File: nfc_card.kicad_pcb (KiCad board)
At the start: 2 copper layers, 2 parts, among them IC1 NT3H2111W0FHKH

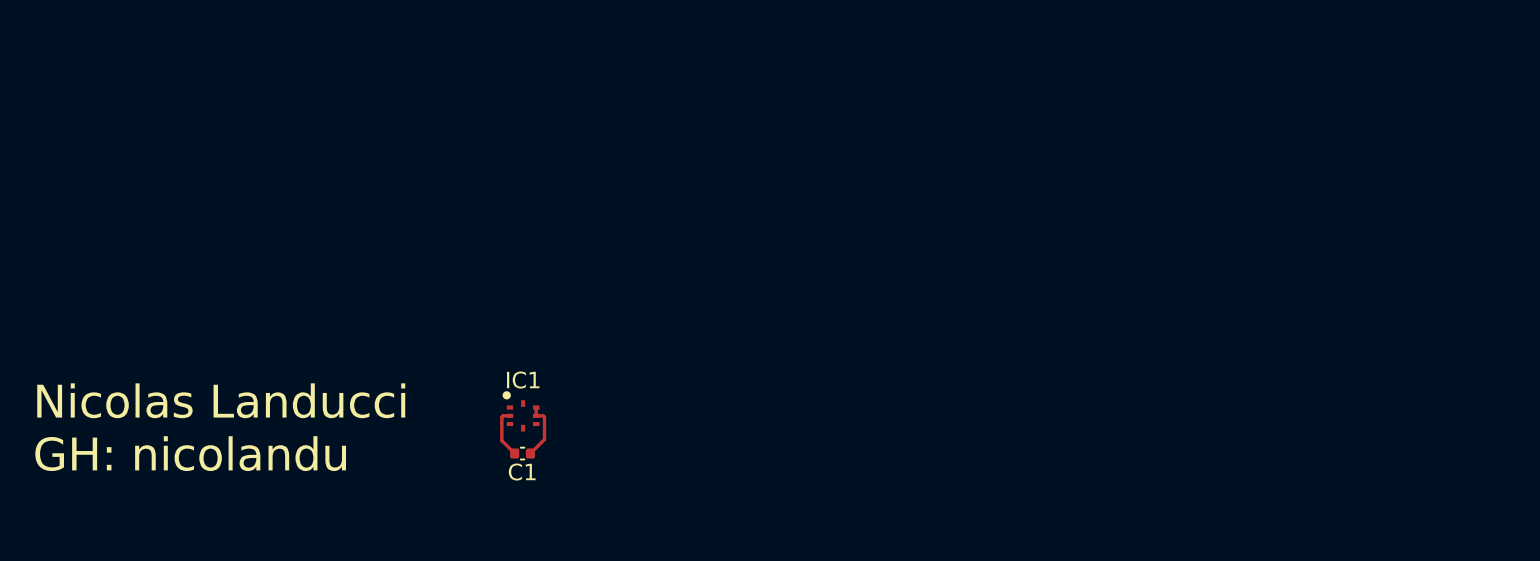
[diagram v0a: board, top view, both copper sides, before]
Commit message: Add antenna
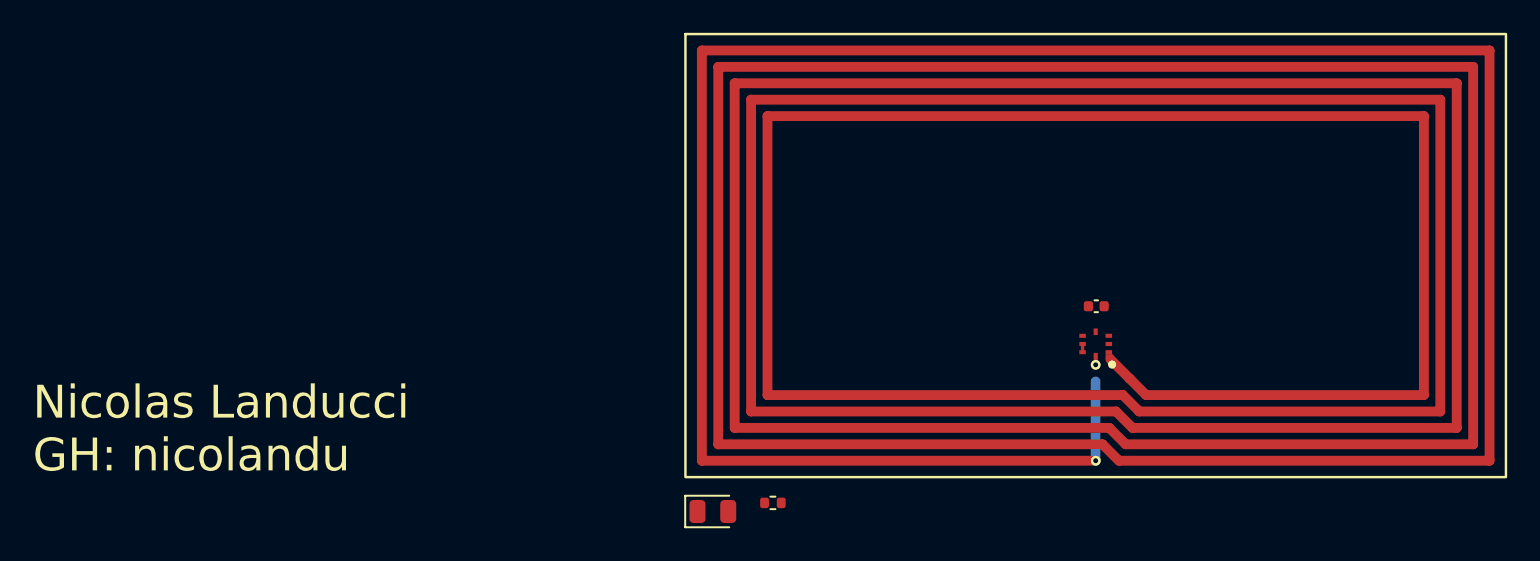
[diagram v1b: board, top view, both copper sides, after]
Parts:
- added AE1: 25x48mm, NFC:Antenna_25x48mm, F.Cu at (121.9, 58.4)
- added D1: LED, LED_SMD:LED_0805_2012Metric, F.Cu at (98.6, 74.0)
- added R1: 47, Resistor_SMD:R_0402_1005Metric, F.Cu at (102.2, 73.5)
- moved C1 36.1 mm to (122.0, 61.5), turned to 0 degrees
- moved IC1 35.2 mm to (121.9, 63.8), turned to 180 degrees
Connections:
- IC1 pad 1: Net-(IC1-LA) -> /ANT1
- IC1 pad 8: Net-(IC1-LA) -> /ANT2
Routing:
- net /ANT2: track 0.00 -> 5.35 mm, vias 0 -> 2
- net Net-(IC1-VCC): track 3.61 -> 0.50 mm
- net Net-(D1-K): track 3.08 -> 0.00 mm
- net /ANT1: track 0.00 -> 1.66 mm

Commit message: Finish wiring
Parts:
- added REF**: MountingHole_8.4mm_M8_Pad, MountingHole:MountingHole_8.4mm_M8_Pad, F.Cu at (132.1, 58.4)
- moved D1 27.4 mm to (121.9, 59.7), turned to 180 degrees
- moved R1 22.2 mm to (121.0, 61.6), turned to 180 degrees
- moved C1 0.93 mm to (122.9, 61.6)
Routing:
- net Net-(D1-K): track 0.00 -> 4.72 mm
- net Net-(IC1-VCC): track 0.50 -> 3.94 mm
- net Net-(D1-A): track 0.00 -> 2.12 mm
- net /ANT2: track 5.35 -> 6.36 mm
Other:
- board outline added: 49.3 x 26.4 mm
- board text added: "NFC"
- board text added: "Nicolas Landucci"
- board text added: "Tapez-moi! Tap me!"
- board text added: "nicolandu"
- board text removed: "Nicolas Landucci GH: nicolandu"
